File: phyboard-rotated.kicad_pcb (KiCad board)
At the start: 2 copper layers, 52 x 41 mm, 32 parts, among them J1 PULSE-J0006, P1 CONN_6X2, U1 TLK110, X1 ASEMB-50.000MHZ-LC-T

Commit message: Using standard QFP50P900X900-48M for the PHY footprint
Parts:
- U1: footprint QFP50P900X900-48N -> QFP50P900X900-48M

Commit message: Laying out rev D
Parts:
- removed hole: VAL**, hole
- added G***: LOGO, LOGO, F.Cu at (171.4, 54.4)
- C6: moved to F.Cu
- moved R1 8.06 mm to (170.0, 66.0), turned to 90 degrees
- moved R5 6.00 mm to (177.0, 30.0), turned to 0 degrees
- moved C10 4.57 mm to (180.0, 38.0), turned to 270 degrees
- moved D3 4.00 mm to (182.0, 30.0), turned to 180 degrees
- moved C6 3.79 mm to (172.0, 30.0)
- moved C11 2.71 mm to (174.0, 41.0), turned to 90 degrees
- moved C13 2.20 mm to (183.0, 34.0)
- moved C12 1.90 mm to (182.0, 38.0), turned to 270 degrees
- moved C8 1.31 mm to (176.0, 36.0)
- moved C1 1.22 mm to (176.0, 42.0), turned to 90 degrees
- moved C15 1.00 mm to (170.0, 57.0)
- moved C9 0.38 mm to (184.0, 38.0), turned to 270 degrees
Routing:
- net GND: track 3.52 -> 194.0 mm, vias 1 -> 9
- net +3.3V: track 19.2 -> 189.5 mm, vias 1 -> 9
- net /ETH_TxD0: track 7.94 -> 56.7 mm, vias 1 -> 2
- net /ETH_TX_EN: track 6.54 -> 51.6 mm, vias 1 -> 2
- net /ETH_CRS: track 1.78 -> 46.1 mm
- net /ETH_MDC: track 0.00 -> 40.1 mm, vias 0 -> 1
- net /ETH_RxD0: track 1.98 -> 41.3 mm
- net /ETH_RxD1: track 1.77 -> 38.8 mm
- net /ETH_MDIO: track 0.00 -> 36.5 mm, vias 0 -> 1
- net /ETH_TxD1: track 14.5 -> 51.0 mm, vias 1 -> 2
- net /ETH_CLK: track 0.00 -> 33.5 mm, vias 0 -> 1
- net N-0000037: track 0.00 -> 32.2 mm, vias 0 -> 1
- net N-0000039: track 0.00 -> 31.2 mm, vias 0 -> 1
- net /PFB: track 0.00 -> 22.7 mm, vias 0 -> 3
- net N-0000038: track 3.23 -> 18.3 mm, vias 0 -> 2
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- added copper zone on B.Cu, net GND
- added copper zone on F.Cu, net GND
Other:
- board size 52 x 41 mm -> 41 x 41 mm
- board text added: "100M"
- board text added: "Ethernet PHY board rev.D Norling 2014"
- board text removed: "3V"
- board text removed: "CLK"
- board text removed: "CRS"
- board text removed: "Ethernet PHY board rev.C Norling 2013"
- board text removed: "MDC"
- board text removed: "MDIO"
- board text removed: "R0"
- board text removed: "R1"
- board text removed: "RD"
- board text removed: "RXERR"
- board text removed: "T0"
- board text removed: "T1"
- board text removed: "TD"
- board text removed: "TXEN"
- board text removed: "rev.D"

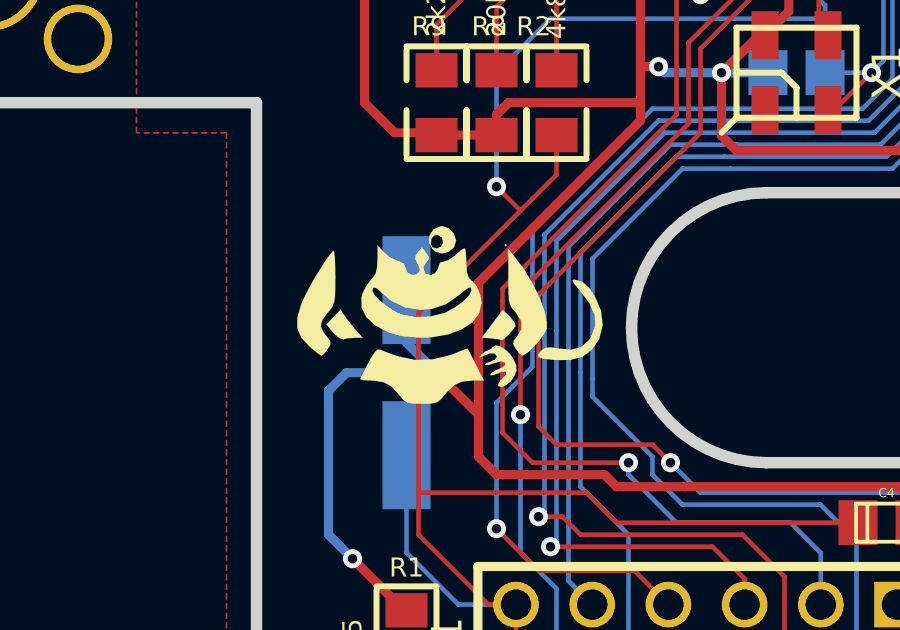
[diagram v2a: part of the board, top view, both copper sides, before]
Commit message: New rev.D with moved monkey
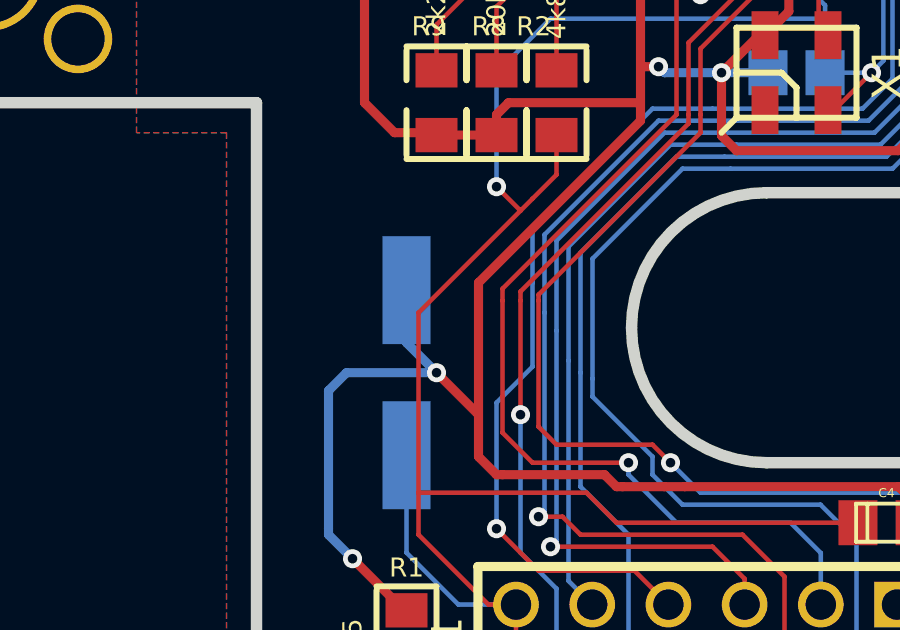
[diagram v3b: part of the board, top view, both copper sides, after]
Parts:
- G***: moved to B.Cu
- moved G*** 7.86 mm to (169.4, 46.8), turned to 90 degrees
